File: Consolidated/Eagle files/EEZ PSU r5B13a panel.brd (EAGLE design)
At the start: 337 x 150 mm, 827 parts, among them IC1 LTC3864EMSE#PBF, IC10 DAC8552IDGKTG4, IC11 ADG465SOT-23, IC12 TS5A9411DCKT, IC13 ADS1120IPWR, IC14 LP339D, IC15 TPD4E002DRL, IC16 TPD2E001DZDR, IC17 ADUM3160BRWZ, IC18 TLC5925IDBQR, IC19 Si8641EC-B-IS1, IC2 LP2951SO8, IC20 SI8651EC-B-IS1, IC21 SI8651EC-B-IS1, IC22 LD1117ADT33TR, IC23 Si8641EC-B-IS1, IC24 PCA21125T/Q900/1,1, IC25 AT25256B-SSHL-B, IC26 W5500, IC27 BC857BS, IC28 TLC555, IC29 SN74LVC08APWR, IC3 TL783CKTTR, IC30 SN74LV1T34DBVR, IC31 TPS3705-33D, IC32 SN74LVC2G02DCTR, IC33 74LVC1G125GW.125, IC34 TPA6205A1DGN, IC35 DAC8552IDGKTG4, IC36 ADS1120IPWR, IC37 LTC2050HVCS8#PBF, IC38 TL072D, IC39 TL072D, IC4 LTC3260EMSE#PBF, IC40 REF5025AIDG4, IC41 LTC3864EMSE#PBF, IC42 TS5A9411DCKT, IC43 ADG465SOT-23, IC44 LP339D, IC45 LTC3260EMSE#PBF, IC46 LP2951SO8, IC47 MCP23S17-E/SS, IC48 TL783CKTTR, IC5 TL072D, IC6 TL072D, IC7 LTC2050HVCS8#PBF, IC8 MCP23S17-E/SS, IC9 REF5025AIDG4, J1 BS-244DSM-R, J2 1-726388-2, J3 BS-244DSM-G, J4 BS-244DSM-B, J5 BS-244DSM-R, J6 BS-244DSM-B, J7 693072010801, Q1 IRFR5305, Q10 MMBT5401, Q11 MMBT5551, Q12 MMBT5551, Q13 IRLL2705PBF, Q14 IRFR48ZPBF, Q15 IRLML2246TRPBF, Q16 2N7002, Q17 MMBT5551, Q18 MMBT5401, Q19 MMBT5551, Q2 MMBT5401, Q20 MMBT5551, Q21 BTA26-600, Q22 BTA26-600, Q23 IRLL2705PBF, Q24 2N7002, Q25 2N7002, Q26 IRLML2246TRPBF, Q27 IRLML2246TRPBF, Q28 IRLML2246TRPBF, Q29 IRLML2246TRPBF, Q3 2N7002, Q30 2N7002, Q31 IRLML2246TRPBF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

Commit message: minor change on AUX PS PCB bottom layer
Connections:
- new net +5V2: C80.1, C81.1, D12.C, IC17.16, K_DOUT.A1, OK1.1, OK2.1, OK3.4, TR1.4, X5.10, X5.8
- new net GND7: C80.2, C81.2, C84.2, IC15.2, IC17.15, IC17.9, JP9.3, Q25.2, R118.2, R122.2, R123.1, TR1.3, X10.4, X5.1, X5.2, X5.9
- net +5V: no longer C80.1, C81.1, D12.C, IC17.16, K_DOUT.A1, OK1.1, OK2.1, OK3.4, TR1.4, X5.10, X5.8
- net GND: no longer C80.2, C81.2, C84.2, IC15.2, IC17.15, IC17.9, JP9.3, Q25.2, R118.2, R122.2, R123.1, TR1.3, X10.4, X5.1, X5.2, X5.9
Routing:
- net +5V: track 967.6 -> 836.9 mm, vias 23 -> 20
- net +5V2: track 0.00 -> 130.7 mm, vias 0 -> 3
- net GND7: track 0.00 -> 14.3 mm, vias 0 -> 9
- net GND: track 449.2 -> 434.9 mm, vias 402 -> 393
- net AC_NEUTRAL: track 102.8 -> 101.2 mm
- added copper zone on layer 16, net GND7
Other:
- board text added: "(11/2017)"
- board text added: "EEZ AUX PS r5B13 (11/2017)"
- board text removed: "(09/2017)"
- board text removed: "EEZ AUX PS r5B13 (09/2017)"

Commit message: JP9, JP10 changed to THT
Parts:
- JP10, JP9: value 0R-JUMPA -> ZL303-03P; device jump-0r-smd:A0R-JMP -> EEZ_Lib1:ZL303-03P
- moved JP10 0.60 mm to (45.7, 62.7), turned to 0 degrees
- moved JP9 0.14 mm to (27.0, 64.5), turned to 270 degrees
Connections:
- removed net +5V2: C80.1, C81.1, D12.C, IC17.16, K_DOUT.A1, OK1.1, OK2.1, OK3.4, TR1.4, X5.10, X5.8
- removed net GND7: C80.2, C81.2, C84.2, IC15.2, IC17.15, IC17.9, JP9.3, Q25.2, R118.2, R122.2, R123.1, TR1.3, X10.4, X5.1, X5.2, X5.9
- net +5V: now also C80.1, C81.1, D12.C, IC17.16, K_DOUT.A1, OK1.1, OK2.1, OK3.4, TR1.4, X5.10, X5.8
- net GND: now also C80.2, C81.2, C84.2, IC15.2, IC17.15, IC17.9, JP9.3, Q25.2, R118.2, R122.2, R123.1, TR1.3, X10.4, X5.1, X5.2, X5.9
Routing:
- net +5V: track 836.9 -> 967.6 mm, vias 20 -> 23
- net +5V2: track 130.7 -> 0.00 mm, vias 3 -> 0
- net GND7: track 14.3 -> 0.00 mm, vias 9 -> 0
- net GND: track 434.9 -> 448.1 mm, vias 393 -> 401
- net XUSB_GND: vias 7 -> 6
- removed copper zone on layer 16, net GND7
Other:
- board text added: "EEZ AUX PS r5B13a"
- board text added: "EEZ AUX PS r5B13a (11/2017)"
- board text added: "EEZ Arduino shield (11/2017 r5B13a)"
- board text added: "USB X10"
- board text removed: "EEZ AUX PS r5B13 (11/2017)"
- board text removed: "EEZ Arduino shield (11/2017 r5B13)"
- board text removed: "USB (isolated) X10"

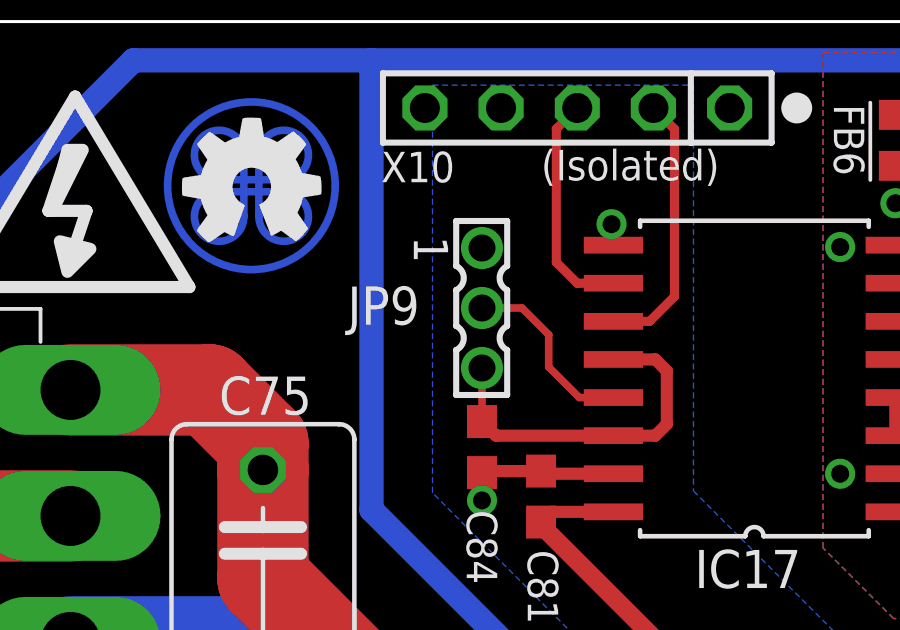
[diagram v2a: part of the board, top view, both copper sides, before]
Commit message: JP9 relocated
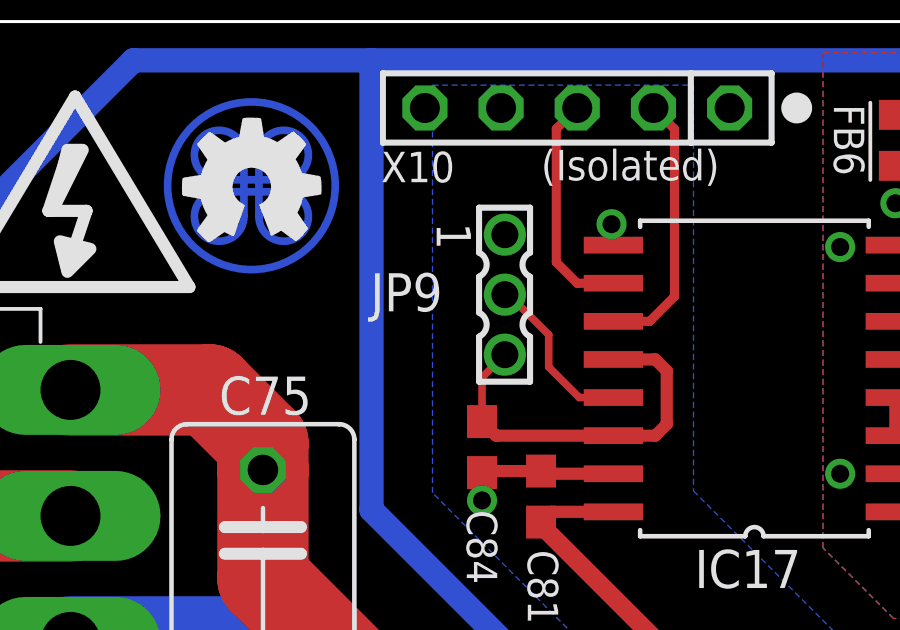
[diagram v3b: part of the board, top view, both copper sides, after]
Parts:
- moved JP9 0.88 mm to (27.7, 64.9)
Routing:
- net N$91: track 12.1 -> 12.8 mm
- net N$105: track 6.25 -> 5.67 mm

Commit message: X1 holes adjustment
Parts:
- D22, D23, D24, D25, D36, D37, D38, D39: device EEZ_Lib1:TO252@1 -> EEZ_Lib1:TO252
- moved X1 4.20 mm to (156.4, 85.8)
- moved X23 4.20 mm to (323.4, 85.8)
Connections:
- new net +5V2: C164.1, C166.2, C186.2, FB10.P$2, IC36.13, IC47.9, Q37.B, Q44.2, R192.2, R193.2, R219.1, R258.2, X21.2
- new net EARTH2: C213.1, C214.2, R270.2, X23.1
- new net GND7: C157.1, C159.1, C161.2, C162.1, C163.1, C164.2, C165.1, C166.1, C167.1, C172.1, C173.2, C177.2, C178.2, C179.1, C180.1, C181.1, C182.1, C183.1, C184.1, C185.1, C186.1, C187.2, C188.2, C189.2, C190.2, C192.2, C193.2, C196.2, C199.2, C200.1, C201.1, C202.2, C204.2, C205.-, C206.-, C207.-, C214.1, C216.1, C217.1, C218.1, C219.1, C220.2, C221.2, C224.1, C225.2, C227.2, C230.2, C231.1, C232.-, C233.+, C234.2, C235.2, C236.-, C237.-, D34.1, D34.2, D38.1, D38.2, D39.1, D39.2, IC35.8, IC36.3, IC36.4, IC36.5, IC36.8, IC40.4, IC41.TP, IC42.3, IC45.14, IC45.17, IC45.2, IC46.4, IC47.10, IC47.15, IC47.16, IC47.17, JP7.3, L9.2, LED1.C, Q43.2, Q45.2, Q51.E, Q52.E, R189.1, R205.1, R213.1, R218.1, R230.2, R234.1, R242.2, R244.1, R246.2, R256.1, R259.1, R267.1, R272.2, R277.1, R278.1, R280.2, R283.2, R286.1, SH4.P$2, SH5.P$2, X21.10, X21.12, X21.14, ZD20.A, ZD21.A
- net +5V: no longer C54.1, C63.2, C64.2, FB1.P$2, IC13.13, IC8.9, Q12.B, Q15.2, R73.1, R84.2, R94.2, R97.2, X2.2
- net +5V1: now also C54.1, C63.2, C64.2, FB1.P$2, IC13.13, IC8.9, Q12.B, Q15.2, R73.1, R84.2, R94.2, R97.2, X2.2; no longer C164.1, C166.2, C186.2, FB10.P$2, IC36.13, IC47.9, Q37.B, Q44.2, R192.2, R193.2, R219.1, R258.2, X21.2
- net EARTH: no longer C2.2, C4.1, R2.2, X1.1
- net EARTH1: now also C2.2, C4.1, R2.2, X1.1; no longer C213.1, C214.2, R270.2, X23.1
- net GND: no longer C10.2, C142.2, C145.-, C146.-, C147.2, C15.2, C16.2, C2.1, C20.2, C21.-, C22.2, C23.-, C24.2, C25.1, C27.-, C28.1, C29.2, C3.2, C30.1, C31.+, C32.2, C33.2, C35.2, C42.1, C43.2, C44.1, C45.1, C46.1, C47.1, C48.1, C49.2, C5.2, C50.1, C51.1, C54.2, C55.2, C56.1, C57.-, C58.2, C59.1, C6.2, C60.1, C61.2, C62.1, C63.1, C64.1, C65.1, C66.1, C67.1, C68.1, C69.1, C72.1, C73.1, C8.2, D1.1, D1.2, D22.1, D22.2, D24.1, D24.2, IC1.TP, IC10.8, IC12.3, IC13.3, IC13.4, IC13.5, IC13.8, IC2.4, IC4.14, IC4.17, IC4.2, IC8.10, IC8.15, IC8.16, IC8.17, IC9.4, JP2.3, L1.2, LED.C, Q16.2, Q17.E, Q19.E, Q7.2, R100.1, R168.2, R18.2, R180.1, R22.2, R23.1, R24.2, R31.2, R45.1, R46.1, R48.1, R66.1, R67.1, R75.1, R86.1, R9.1, R90.1, R91.2, SH1.P$2, SH2.P$2, X2.10, X2.12, X2.14, ZD1.A, ZD16.A
- net GND1: now also C10.2, C142.2, C145.-, C146.-, C147.2, C15.2, C16.2, C2.1, C20.2, C21.-, C22.2, C23.-, C24.2, C25.1, C27.-, C28.1, C29.2, C3.2, C30.1, C31.+, C32.2, C33.2, C35.2, C42.1, C43.2, C44.1, C45.1, C46.1, C47.1, C48.1, C49.2, C5.2, C50.1, C51.1, C54.2, C55.2, C56.1, C57.-, C58.2, C59.1, C6.2, C60.1, C61.2, C62.1, C63.1, C64.1, C65.1, C66.1, C67.1, C68.1, C69.1, C72.1, C73.1, C8.2, D1.1, D1.2, D22.1, D22.2, D24.1, D24.2, IC1.TP, IC10.8, IC12.3, IC13.3, IC13.4, IC13.5, IC13.8, IC2.4, IC4.14, IC4.17, IC4.2, IC8.10, IC8.15, IC8.16, IC8.17, IC9.4, JP2.3, L1.2, LED.C, Q16.2, Q17.E, Q19.E, Q7.2, R100.1, R168.2, R18.2, R180.1, R22.2, R23.1, R24.2, R31.2, R45.1, R46.1, R48.1, R66.1, R67.1, R75.1, R86.1, R9.1, R90.1, R91.2, SH1.P$2, SH2.P$2, X2.10, X2.12, X2.14, ZD1.A, ZD16.A; no longer C157.1, C159.1, C161.2, C162.1, C163.1, C164.2, C165.1, C166.1, C167.1, C172.1, C173.2, C177.2, C178.2, C179.1, C180.1, C181.1, C182.1, C183.1, C184.1, C185.1, C186.1, C187.2, C188.2, C189.2, C190.2, C192.2, C193.2, C196.2, C199.2, C200.1, C201.1, C202.2, C204.2, C205.-, C206.-, C207.-, C214.1, C216.1, C217.1, C218.1, C219.1, C220.2, C221.2, C224.1, C225.2, C227.2, C230.2, C231.1, C232.-, C233.+, C234.2, C235.2, C236.-, C237.-, D34.1, D34.2, D38.1, D38.2, D39.1, D39.2, IC35.8, IC36.3, IC36.4, IC36.5, IC36.8, IC40.4, IC41.TP, IC42.3, IC45.14, IC45.17, IC45.2, IC46.4, IC47.10, IC47.15, IC47.16, IC47.17, JP7.3, L9.2, LED1.C, Q43.2, Q45.2, Q51.E, Q52.E, R189.1, R205.1, R213.1, R218.1, R230.2, R234.1, R242.2, R244.1, R246.2, R256.1, R259.1, R267.1, R272.2, R277.1, R278.1, R280.2, R283.2, R286.1, SH4.P$2, SH5.P$2, X21.10, X21.12, X21.14, ZD20.A, ZD21.A
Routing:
- net +5V: track 967.6 -> 744.0 mm, vias 23 -> 20
- net +5V2: track 0.00 -> 223.6 mm, vias 0 -> 3
- net GND7: track 0.00 -> 185.7 mm, vias 0 -> 139
- net GND: track 448.1 -> 262.5 mm, vias 401 -> 262
- net EARTH2: track 0.00 -> 41.2 mm
- net EARTH: track 325.0 -> 284.0 mm
- added copper zone on layer 1, net GND7
- added copper zone on layer 16, net GND7
- added copper zone on layer 1, net N$273
- added copper zone on layer 1, net N$46
- removed copper zone on layer 1, net N$24
- removed copper zone on layer 1, net N$272 (its old number)

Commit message: #64, #65
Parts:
- removed IC47: MCP23S17-E/SS, EEZ_Lib1:SOP65P780X200-28N
- removed IC48: TL783CKTTR, EEZ_Lib1:TO254P1524X483-4N
- removed LED, LED1: n.c., EEZ_Lib1:LED_HSMH-C170
- removed R283: 1K8, rcl:R0805
- removed R284: 0R082, rcl:R1210
- removed R285: 0R75?, rcl:R1206
- removed R286: 47K, rcl:R0805
- added R78A, R78A1, R78B, R78B1: 470R, rcl:R0805
- added ZD22: SMAJ51A, EEZ_Lib1:DO214AA
- added ZD23: PDZ5.6B, EEZ_Lib1:SOD323-W
- added ZD24: SLVU2.8-TP, EEZ_Lib1:SOT23
- C206, C57: value 10u -> 4u7
- C231, C62: value n.c. -> 10n
- D10, D13, D16, D2, D21, D26, D27, D28, D29, D3, D30, D31, D32, D33, D35, D4, D5, D6, D7, D8, D9: device diode:SOD323-W -> EEZ_Lib1:SOD323-R
- IC11: value ADG465SOT-23 -> DAC8552IDGKTG4; device EEZ_Lib1:SOT95P280X145-6N -> EEZ_Lib1:DGK8-M
- IC35: value DAC8552IDGKTG4 -> ADS1120IPWR; device EEZ_Lib1:DGK8-M -> EEZ_Lib1:PW(R-PDSO-G16)
- IC36: value ADS1120IPWR -> LTC2050HVCS8#PBF; device EEZ_Lib1:PW(R-PDSO-G16) -> EEZ_Lib1:SOIC127P600X173-8N
- IC37: value LTC2050HVCS8#PBF -> TL072D
- IC39: value TL072D -> REF5025AIDG4; device EEZ_Lib1:SOIC127P600X173-8N -> EEZ_Lib1:SOIC127P600X175-8N
- IC40: value REF5025AIDG4 -> LTC3864EMSE#PBF; device EEZ_Lib1:SOIC127P600X175-8N -> EEZ_Lib1:LTC_05-08-1666
- IC41: value LTC3864EMSE#PBF -> TS5A9411DCKT; device EEZ_Lib1:LTC_05-08-1666 -> EEZ_Lib1:SOT65P210X110-6N
- IC42: value TS5A9411DCKT -> LP339D; device EEZ_Lib1:SOT65P210X110-6N -> EEZ_Lib1:SOIC127P600X175-14N
- IC43: value ADG465SOT-23 -> LTC3260EMSE#PBF; device EEZ_Lib1:SOT95P280X145-6N -> EEZ_Lib1:SOP50P490X110-17N
- IC44: value LP339D -> LP2951SO8; device EEZ_Lib1:SOIC127P600X175-14N -> EEZ_Lib1:SOIC127P600X175-8N
- IC45: value LTC3260EMSE#PBF -> MCP23S17-E/SS; device EEZ_Lib1:SOP50P490X110-17N -> EEZ_Lib1:SOP65P780X200-28N
- IC46: value LP2951SO8 -> TL783CKTTR; device EEZ_Lib1:SOIC127P600X175-8N -> EEZ_Lib1:TO254P1524X483-4N
- JP1, JP2, JP3, JP4, JP5, JP6, JP7: value 0R-JUMPA -> JP3-CUT; device jump-0r-smd:A0R-JMP -> EEZ_Lib1:JP3-CUT
- R1, R183, R184, R270: value n.c. -> 10K
- R179: value 0R75? -> 0R75
- R181: value 10K -> n.c.
- R182, R267: value 2K2 -> n.c.
- R185: value 10K -> 10R; device rcl:R0805 -> rcl:R1206
- R187: value 10R -> 2K2; device rcl:R1206 -> rcl:R0805
- R188: value 10K -> 5K6
- R189: value 2K2 -> 5K6
- R190, R191: value 5K6 -> 5K1
- R192, R193: value 5K1 -> 10K
- R196, R197, R214, R257, R258: value 10K -> 220R
- R198: value 220R -> 470R
- R199: value 220R -> 100R
- R200: value 470R -> 1K
- R201: value 100R -> 470R
- R202: value 1K -> 16K
- R203: value 470R -> 750R
- R204: value 16K -> 2K2
- R205: value 750R -> 2K2
- R206: value 2K2 -> 220R
- R207: value 2K2 -> 1K
- R208, R272: value 220R -> 47K
- R209: value 1K -> 10K
- R210, R238, R255: value 47K -> 10K
- R211: value 10K -> 100K
- R213: value 100K -> 220R
- R215: value 220R -> 1K8
- R216: value 220R -> 51K
- R217: value 1K8 -> 100K
- R218: value 51K -> 7K5 0.1%
- R219: value 100K -> 100K 0.1%
- R220: value 7K5 0.1% -> 100K 0.1%
- R221, R222: value 100K 0.1% -> 24K 0.1%
- R223: value 24K 0.1% -> 7K5 0.1%
- R224: value 24K 0.1% -> 3K9 0.1%
- R225: value 7K5 0.1% -> 82R 0.1%
- R226: value 3K9 0.1% -> 82R 0.1%
- R227: value 82R 0.1% -> 3K9 0.1%
- R228: value 82R 0.1% -> 10K
- R229: value 3K9 0.1% -> 0R
- R230: value 10K -> 316K
- R231: value 0R -> 4K7
- R232: value 316K -> 10R; device rcl:R0805 -> rcl:R1206
- R233: value 4K7 -> 100K
- R234: value 10R -> 10K; device rcl:R1206 -> rcl:R0805
- R236, R273, R281: value 10K -> 47K
- R237: value 100K -> R010/2W; device rcl:R0805 -> rcl:R2512
- R239: value R010/2W -> 100R; device rcl:R2512 -> rcl:R0805
- R240: value 10K -> 12K; device rcl:R0805 -> rcl:R1206
- R241: value 100R -> 316K
- R242: value 12K -> 100K; device rcl:R1206 -> rcl:R0805
- R243: value 316K -> 100K
- R244: value 100K -> 10K
- R245: value 1K -> n.c.
- R246: value 100K -> 100R
- R247: value 10K -> 330R
- R248: value n.c. -> 750R
- R249: value 100R -> 1K
- R252: value 1K -> 47K
- R253: value 330R -> 47K
- R254: value 750R -> 10K
- R259, R277: value 47K -> 220R
- R261: value 220R -> 2R2/2W; device rcl:R0805 -> rcl:R2512
- R262: value 220R -> 316K
- R263: value 220R -> 1K
- R264: value 2R2/2W -> 2K2; device rcl:R2512 -> rcl:R0805
- R265: value 316K -> 2K2
- R266: value 1K -> 10R; device rcl:R0805 -> rcl:R1206
- R268: value 2K2 -> n.c.; device rcl:R0805 -> rcl:R1206
- R269: value 10R -> 220R; device rcl:R1206 -> rcl:R0805
- R271: value n.c. -> 1R; device rcl:R1206 -> rcl:R0805
- R274: value 1R -> 16K
- R275: value n.c. -> 5K1
- R276: value 0R030 -> 10K; device EEZ_Lib1:R_2512-4WIRE -> rcl:R0805
- R278: value 47K -> 1K8
- R279: value 16K -> 0R082; device rcl:R0805 -> rcl:R1210
- R280: value 5K1 -> 0R75; device rcl:R0805 -> rcl:R1206
- R282: value 220R -> 0R030; device rcl:R0805 -> rcl:R2512
- R65, R65B, R65B1: device EEZ_Lib1:R_2512-4WIRE -> rcl:R2512
- R78: value 1K -> 2K2
- ZD17: value BZX384-C15 -> PDZ5.6B
- ZD18: value PDZ6.2B -> SLVU2.8-TP; device EEZ_Lib1:SOD323-W -> EEZ_Lib1:SOT23
- ZD19: value n.c. -> BZX384-C15; device EEZ_Lib1:DO214AA -> EEZ_Lib1:SOD323-W
- ZD20: value SMAJ51A -> PDZ6.2B; device EEZ_Lib1:DO214AA -> EEZ_Lib1:SOD323-W
- ZD21: value PDZ5.6B -> n.c.; device EEZ_Lib1:SOD323-W -> EEZ_Lib1:DO214AA
- moved ZD18 208.6 mm to (31.9, 124.8), turned to 180 degrees
- moved IC11 199.3 mm to (230.3, 138.7), turned to 180 degrees
- moved ZD17 191.8 mm to (51.6, 60.1), turned to 270 degrees
- moved R78 183.2 mm to (209.4, 107.9)
- moved R268 126.1 mm to (308.7, 133.6), flipped to the bottom, turned to 180 degrees
- moved R270 117.0 mm to (198.7, 116.3), turned to 180 degrees
- moved R249 106.4 mm to (182.5, 135.7), turned to 180 degrees
- moved R280 101.2 mm to (198.2, 92.7), turned to 270 degrees
- moved ZD19 100.7 mm to (242.2, 81.9), turned to 0 degrees
- moved R278 97.7 mm to (279.1, 138.8), turned to 180 degrees
- moved R281 96.1 mm to (192.8, 93.5), turned to 180 degrees
- moved R279 95.9 mm to (202.2, 90.7), turned to 180 degrees
- moved R248 93.6 mm to (185.7, 98.0), turned to 0 degrees
- moved R277 92.2 mm to (276.9, 135.3), turned to 90 degrees
- moved R266 90.4 mm to (268.6, 78.9), turned to 180 degrees
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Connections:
- removed net +5V2: C164.1, C166.2, C186.2, FB10.P$2, IC36.13, IC47.9, Q37.B, Q44.2, R192.2, R193.2, R219.1, R258.2, X21.2
- removed net EARTH2: C213.1, C214.2, R270.2, X23.1
- removed net GND7: C157.1, C159.1, C161.2, C162.1, C163.1, C164.2, C165.1, C166.1, C167.1, C172.1, C173.2, C177.2, C178.2, C179.1, C180.1, C181.1, C182.1, C183.1, C184.1, C185.1, C186.1, C187.2, C188.2, C189.2, C190.2, C192.2, C193.2, C196.2, C199.2, C200.1, C201.1, C202.2, C204.2, C205.-, C206.-, C207.-, C214.1, C216.1, C217.1, C218.1, C219.1, C220.2, C221.2, C224.1, C225.2, C227.2, C230.2, C231.1, C232.-, C233.+, C234.2, C235.2, C236.-, C237.-, D34.1, D34.2, D38.1, D38.2, D39.1, D39.2, IC35.8, IC36.3, IC36.4, IC36.5, IC36.8, IC40.4, IC41.TP, IC42.3, IC45.14, IC45.17, IC45.2, IC46.4, IC47.10, IC47.15, IC47.16, IC47.17, JP7.3, L9.2, LED1.C, Q43.2, Q45.2, Q51.E, Q52.E, R189.1, R205.1, R213.1, R218.1, R230.2, R234.1, R242.2, R244.1, R246.2, R256.1, R259.1, R267.1, R272.2, R277.1, R278.1, R280.2, R283.2, R286.1, SH4.P$2, SH5.P$2, X21.10, X21.12, X21.14, ZD20.A, ZD21.A
- removed net N$206 (its old number): C176.2, R199.1
- removed net N$269: LED1.A, R275.1
- removed net N$276: IC48.1, R282.2, R283.1
- removed net N$277: R276.2S, R284.1, R65A1.2S, R65B1.2S
- removed net N$278: Q55.2, R227.1, R285.1
- removed net N$78 (its old number): LED.A, R1.1
- removed net N$9 (its old number): IC11.4, IC12.6
- new net N$105: IC38.3, R78.2
- new net N$106: IC37.3, R183.2, R196.2
- new net N$210: D31.C, ZD19.C
- new net N$273: R279.1, R65A1.2S
- new net N$70: R63.1, R65A.2S
- net !DP_DRIVE1: now also R207.1, R212.1; no longer R209.1, R214.1
- net !INT: now also JP3.COM; no longer JP3.2
- net !INT1: now also JP7.COM; no longer JP6.2
- net !PS_DRDY: now also JP3.NC; no longer JP3.3
- net !PS_DRDY1: now also IC35.14, JP7.NC; no longer IC36.14, JP6.3
- net !PS_RESET1: now also IC45.18; no longer IC47.18
- net !SET_100%1: now also IC45.24; no longer IC47.24
- net !SET_DP1: now also IC45.22, R217.2; no longer IC47.22, R219.2
- net +3V3: now also JP4.NO; no longer JP4.3
- net +5V: now also C54.1, C63.2, C64.2, FB1.P$2, IC13.13, IC8.9, JP4.NC, Q12.B, Q15.2, R73.1, R84.2, R94.2, R97.2, X2.2; no longer JP4.1
- net +5V1: now also C164.1, C166.2, C186.2, FB10.P$2, IC35.13, IC45.9, Q37.B, Q44.2, R190.2, R191.2, R217.1, R255.2, X21.2; no longer C54.1, C63.2, C64.2, FB1.P$2, IC13.13, IC8.9, Q12.B, Q15.2, R73.1, R84.2, R94.2, R97.2, X2.2
- net +VNR1: now also IC43.1, IC43.11, IC43.13, IC44.8, IC46.2, IC46.4, R277.1; no longer IC45.1, IC45.11, IC45.13, IC46.8, IC48.2, IC48.4, R282.1
- net +VREF1: now also IC11.2, IC35.9, IC39.6, R270.1; no longer IC35.2, IC36.9, IC40.6, R273.1
- net -12V1: now also IC43.6, R206.2, R207.2; no longer IC45.6, R208.2, R209.2
- net -5VOUT1: now also IC43.5, R262.2; no longer IC45.5, R265.2
- net AC_IN3: now also ZD21.C; no longer ZD19.C
- net AC_IN4: now also R268.2, ZD21.A; no longer R271.2, ZD19.A
- net AUX_ETH_OUT+: now also IC15.3; no longer IC15.1
- net AUX_ETH_OUT-: now also IC15.1; no longer IC15.3
- net AUX_USET_IN: now also R78A.2; no longer R78.2
- net AUX_USET_IN1: now also R78A1.2; no longer R245.2
- net AUX_USET_SW1: now also IC41.1, IC45.25; no longer IC42.1, IC47.25
- net CC_ACTIVE1: now also IC45.23, R189.2, R191.1; no longer IC47.23, R191.2, R193.1
- net CS_ADC1: now also IC35.2; no longer IC36.2
- net CS_DAC1: now also IC11.5; no longer IC35.5
- net CS_EXPANDER1: now also IC45.11; no longer IC47.11
- net CURR_500MA1: now also IC45.2, R273.2; no longer IC47.2, R278.2
- net CURR_50MA1: now also IC45.3, R281.2; no longer IC47.3, R286.2
- net CURR_5A1: now also IC45.1, R272.2; no longer IC47.1, R277.2
- net CV_ACTIVE1: now also IC45.26, R188.2, R190.1; no longer IC47.26, R190.2, R192.1
- net DC_BIAS1: now also R213.2, R214.2, R266.2; no longer R215.2, R216.2, R269.2
- net DC_OUT: no longer R1.2
- net DC_OUT1: now also IC40.11, IC46.3, R237.1, R240.1, R266.1, ZD22.C; no longer IC41.11, IC48.3, R239.1, R242.1, R269.1, R275.2, ZD20.C
- net DP_LED1: now also R212.2; no longer R214.2
- net EARTH: now also C2.2, C4.1, R2.2, X1.1
- net EARTH1: now also C213.1, C214.2, R267.2, X23.1; no longer C2.2, C4.1, R2.2, X1.1
- net FB1: now also IC40.5, R230.2, R231.1, R245.2; no longer IC41.5, R232.2, R233.1, R248.2
- net GCOM: now also JP2.COM; no longer JP2.2
- net GCOM1: now also JP6.COM, R218.1, R224.1; no longer JP7.2, R220.1, R226.1
- net GND: now also C10.2, C142.2, C145.-, C146.-, C147.2, C15.2, C16.2, C2.1, C20.2, C21.-, C22.2, C23.-, C24.2, C25.1, C27.-, C28.1, C29.2, C3.2, C30.1, C31.+, C32.2, C33.2, C35.2, C42.1, C43.2, C44.1, C45.1, C46.1, C47.1, C48.1, C49.2, C5.2, C50.1, C51.1, C54.2, C55.2, C56.1, C57.-, C58.2, C59.1, C6.2, C60.1, C61.2, C62.1, C63.1, C64.1, C65.1, C66.1, C67.1, C68.1, C69.1, C72.1, C73.1, C8.2, D1.1, D1.2, D22.1, D22.2, D24.1, D24.2, IC1.TP, IC10.8, IC12.3, IC13.3, IC13.4, IC13.5, IC13.8, IC2.4, IC4.14, IC4.17, IC4.2, IC8.10, IC8.15, IC8.16, IC8.17, IC9.4, JP2.NO, L1.2, Q16.2, Q17.E, Q19.E, Q7.2, R100.1, R168.2, R18.2, R180.1, R22.2, R23.1, R24.2, R31.2, R45.1, R46.1, R48.1, R66.1, R67.1, R75.1, R86.1, R9.1, R90.1, R91.2, SH1.P$2, SH2.P$2, X2.10, X2.12, X2.14, ZD1.A, ZD16.A, ZD18.1, ZD18.2
- net GND1: now also C157.1, C159.1, C161.2, C162.1, C163.1, C164.2, C165.1, C166.1, C167.1, C172.1, C173.2, C177.2, C178.2, C179.1, C180.1, C181.1, C182.1, C183.1, C184.1, C185.1, C186.1, C187.2, C188.2, C189.2, C190.2, C192.2, C193.2, C196.2, C199.2, C200.1, C201.1, C202.2, C204.2, C205.-, C206.-, C207.-, C214.1, C216.1, C217.1, C218.1, C219.1, C220.2, C221.2, C224.1, C225.2, C227.2, C230.2, C231.1, C232.-, C233.+, C234.2, C235.2, C236.-, C237.-, D34.1, D34.2, D38.1, D38.2, D39.1, D39.2, IC11.8, IC35.3, IC35.4, IC35.5, IC35.8, IC39.4, IC40.TP, IC41.3, IC43.14, IC43.17, IC43.2, IC44.4, IC45.10, IC45.15, IC45.16, IC45.17, JP6.NO, L9.2, Q43.2, Q45.2, Q51.E, Q52.E, R187.1, R203.1, R211.1, R216.1, R228.2, R232.1, R240.2, R242.1, R243.2, R253.1, R256.1, R264.1, R269.2, R272.1, R273.1, R275.2, R278.2, R281.1, SH4.P$2, SH5.P$2, X21.10, X21.12, X21.14, ZD22.A, ZD23.A, ZD24.1, ZD24.2; no longer C10.2, C142.2, C145.-, C146.-, C147.2, C15.2, C16.2, C2.1, C20.2, C21.-, C22.2, C23.-, C24.2, C25.1, C27.-, C28.1, C29.2, C3.2, C30.1, C31.+, C32.2, C33.2, C35.2, C42.1, C43.2, C44.1, C45.1, C46.1, C47.1, C48.1, C49.2, C5.2, C50.1, C51.1, C54.2, C55.2, C56.1, C57.-, C58.2, C59.1, C6.2, C60.1, C61.2, C62.1, C63.1, C64.1, C65.1, C66.1, C67.1, C68.1, C69.1, C72.1, C73.1, C8.2, D1.1, D1.2, D22.1, D22.2, D24.1, D24.2, IC1.TP, IC10.8, IC12.3, IC13.3, IC13.4, IC13.5, IC13.8, IC2.4, IC4.14, IC4.17, IC4.2, IC8.10, IC8.15, IC8.16, IC8.17, IC9.4, JP2.3, L1.2, LED.C, Q16.2, Q17.E, Q19.E, Q7.2, R100.1, R168.2, R18.2, R180.1, R22.2, R23.1, R24.2, R31.2, R45.1, R46.1, R48.1, R66.1, R67.1, R75.1, R86.1, R9.1, R90.1, R91.2, SH1.P$2, SH2.P$2, X2.10, X2.12, X2.14, ZD1.A, ZD16.A
- net HEATSINK1: now also R267.1; no longer R270.1
- net INT_EXP: now also JP3.NO; no longer JP3.1
- net INT_EXP1: now also IC45.20, JP7.NO; no longer IC47.20, JP6.1
- net ISENSE+1: now also IC36.3, R224.2, R225.2; no longer IC37.3, R226.2, R227.2
- net ISENSE-1: now also IC36.2, R226.2, R227.1; no longer IC37.2, R228.2, R229.1
- net I_MON1: now also IC36.6, R1.1, R227.2, R258.1; no longer IC37.6, R181.1, R229.2, R261.1
- net I_SERVO1: now also IC38.1, R210.1; no longer IC39.1, R212.1
- net I_SET1: now also IC11.3, R260.1, R78.1; no longer IC35.3, R182.1, R263.1
- net LOOP_CTRL1: now also R198.1; no longer R200.1
- net L_OUT12: now also R230.1, R234.1, R235.1, R246.1; no longer R232.1, R236.1, R237.1, R249.1
- net MODE: now also JP1.COM; no longer JP1.2
- net MODE1: now also IC40.1, JP5.COM; no longer IC41.1, JP5.2
- net N$102: now also JP4.COM; no longer JP4.2
- net N$104: now also R78A.1, R78B.2; no longer R63.1, R65.2S, R65A.2S, R65B.2S
- net N$12: now also IC12.6, R78B.1, ZD18.3; no longer IC11.1, R78.1
- net N$157: now also C160.1, D27.C, IC37.2, R184.2, R197.2; no longer IC39.3, R182.2
- net N$159: now also C165.2, C185.2, IC35.12; no longer IC38.3, R198.2
- net N$16: now also JP2.NC; no longer JP2.1
- net N$168: now also IC42.1, IC42.2, R188.1; no longer C160.1, D27.C, IC38.2, R186.2, R199.2
- net N$179: now also IC37.5, R192.2, R218.2, R219.1; no longer C165.2, C185.2, IC36.12, R187.2
- net N$180: now also IC37.6, R193.2, R220.1, R223.2; no longer IC44.1, IC44.2, R190.1
- net N$189: now also C171.1, R222.1; no longer IC38.5, R194.2, R221.1
- net N$190: now also C169.1, R219.2, R221.1; no longer IC38.6, R195.2, R222.1, R225.2
- net N$191: now also C168.2, R192.1; no longer C171.1, R222.2, R224.1
- net N$192: now also C170.2, R193.1; no longer C169.1, R221.2, R223.1
- net N$196: now also C174.2, R195.1; no longer C168.2, R194.1
- net N$200: no longer R65.1S, R65B.1S
- net N$202: now also D26.C, IC38.2, R1.2, R194.2, R195.2; no longer C170.2, R195.1
- net N$203: now also C175.2, R196.1; no longer C174.2, R197.1
- net N$204: now also C176.2, R197.1; no longer D26.C, IC39.2, R181.2, R196.2, R197.2
- net N$205: now also D30.C, D32.A, Q35.G, R200.1; no longer C175.2, R198.1
- net N$209: now also D31.A, Q36.1, R199.1, R201.2; no longer D30.C, D32.A, Q35.G, R202.1
- net N$211: now also C177.1; no longer D31.A, Q36.1, R203.2
- net N$212: now also D32.C, ZD20.C; no longer D31.C, ZD17.C
- net N$213: now also Q45.3, R204.1, R205.1, R261.1; no longer C177.1, R203.1
- net N$214: now also D33.A, Q42.C, Q45.1, R205.2; no longer D32.C, ZD18.C
- net N$215: now also Q41.E, R198.2; no longer Q45.3, R206.1, R207.1, R264.1
- net N$216: now also IC42.13, IC42.14, R189.1; no longer D33.A, Q42.C, Q45.1, R207.2
- net N$217: now also IC42.5, IC42.6, R209.2; no longer Q41.E, R200.2
- net N$218: now also IC42.11, IC42.8, R210.2; no longer IC44.13, IC44.14, R191.1
- net N$219: now also IC42.7, IC42.9, R187.2, R208.1; no longer IC44.5, IC44.6, R211.2
- net N$220: now also IC42.10, IC42.4, R186.2, R228.1; no longer IC44.11, IC44.8, R212.2
- net N$221: now also Q40.E, R213.1; no longer IC44.7, IC44.9, R189.2, R210.1
- net N$222: now also Q39.E, R214.1; no longer IC44.10, IC44.4, R188.2, R230.1
- net N$223: now also Q37.E, R215.2; no longer Q40.E, R215.1
- net N$224: now also Q41.B, R202.1, R203.2, R264.2; no longer Q39.E, R216.1
- net N$225: now also Q38.3, R206.1; no longer Q37.E, R217.2
- net N$226: now also Q42.B, R204.2; no longer Q41.B, R204.1, R205.2, R267.2
- net N$227: now also C187.1, IC39.5; no longer Q38.3, R208.1
- net N$228: now also IC38.6, IC38.7, JP6.NC; no longer Q42.B, R206.2
- net N$229: now also C160.2, R229.1; no longer C187.1, IC40.5
- net N$230: now also C191.2, R232.2; no longer IC39.6, IC39.7, JP7.1
- net N$231: now also C209.2, D35.A, Q46.B, R233.1, R235.2; no longer C160.2, R231.1
- net N$232: now also D35.C, Q46.E; no longer C191.2
- net N$233: now also C195.1, IC40.6, R238.2; no longer C209.2, D35.A, Q46.B, R235.1, R237.2
- net N$234: now also C194.1, R238.1; no longer D35.C, Q46.E, R236.2
- net N$235: now also C197.1, IC40.9; no longer C195.1, IC41.6, R240.2
- net N$236: now also IC40.12, R271.1; no longer C194.1, R240.1
- net N$237: now also IC40.2, R236.1; no longer C197.1, IC41.9
- net N$238: now also C198.2, IC40.4; no longer IC41.12, R274.1
- net N$239: now also C209.1, Q46.C, Q48.3, R245.1; no longer IC41.2, R238.1
- net N$240: now also C222.1, L6.1, L7.2, R239.1, R246.2; no longer C198.2, IC41.4
- net N$241: now also C204.1, C232.+, FB9.P$1, IC43.12, R241.1; no longer C209.1, Q46.C, Q48.3, R248.1
- net N$242: now also C231.2, IC41.6, R78B1.1, ZD24.3; no longer C222.1, L6.1, L7.2, R241.1, R249.2
- net N$243: now also IC40.8, R244.1; no longer C204.1, C232.+, FB9.P$1, IC45.12, R243.1
- net N$244: now also C210.2, Q50.B, R247.1, R248.2, R265.2; no longer IC42.6, IC43.4
- net N$245: now also C212.2, Q50.C, R252.1, R254.2; no longer C231.2, IC43.1, R245.1
- net N$246: now also Q49.C, R249.1; no longer IC41.8, R247.1
- net N$247: now also C211.1, Q49.B, R250.2, R251.1; no longer C210.2, Q50.B, R250.1, R251.2, R268.2
- net N$248: now also C212.1, Q51.B, R252.2, R253.2; no longer C212.2, Q50.C, R255.1, R257.2
- net N$249: now also Q52.B, R254.1, R256.2; no longer Q49.C, R252.1
- net N$250: now also C217.2, IC35.10, R257.2; no longer C211.1, Q49.B, R253.2, R254.1
- net N$251: now also C218.2, IC35.7, R258.2; no longer C212.1, Q51.B, R255.2, R256.2
- net N$252: now also C219.2, IC35.11; no longer Q52.B, R257.1
- net N$253: now also C220.1, IC35.6; no longer C217.2, IC36.10
- net N$254: now also R194.1, R263.2; no longer C218.2, IC36.7, R261.2
- net N$255: now also C158.1, R263.1; no longer C219.2, IC36.11, R262.2
- net N$256: now also R249.2, R265.1; no longer C220.1, IC36.6, R263.2
- net N$257: now also C229.2, R268.1; no longer R196.1, R266.2
- net N$258: now also C230.1, IC38.5, R269.1, R270.2; no longer C158.1, R266.1
- net N$259: now also Q47.1, R271.2; no longer R252.2, R268.1
- net N$260: now also IC43.15, R241.2, R243.1; no longer C229.2, R271.1
- net N$261: now also C200.2, IC43.16; no longer C230.1, IC39.5, R272.1, R273.2
- net N$262: now also C201.2, IC43.3; no longer Q47.1, R274.2
- net N$263: now also IC43.4, R242.2, R262.1; no longer IC45.15, R243.2, R246.1
- net N$264: now also C203.1, IC43.10, IC43.9; no longer C200.2, IC45.16
- net N$265: now also C203.2, IC43.7, IC43.8; no longer C201.2, IC45.3
- net N$266: now also Q54.3, R282.2, R65A1.2, R65B1.2; no longer IC45.4, R244.2, R265.1
- net N$267: now also IC44.7, R274.2, R275.1; no longer C203.1, IC45.10, IC45.9
- net N$268: now also C236.+, FB10.P$1, IC44.1, R274.1, R276.1; no longer C203.2, IC45.7, IC45.8
- net N$270: now also R226.1, R65A1.1S; no longer Q54.3, R276.2, R65A1.2, R65B1.2
- net N$271: now also Q53.3, R280.2; no longer IC46.7, R280.1
- net N$272: now also R277.2, R278.1; no longer C236.+, FB10.P$1, R279.1, R281.1
- net N$274: now also Q55.2, R225.1, R280.1; no longer R228.1, R276.1S, R65A1.1S, R65B1.1S
- net N$275: now also R78A1.1, R78B1.2; no longer Q53.3, R284.2, R285.2
- net OUT+1: now also R181.1, R200.2, R233.2, R247.2, R261.2, ZD19.A; no longer R183.1, R204.2, R235.2, R250.2, R264.2, ZD17.A
- net OUT-1: now also R182.2, R250.1; no longer R184.2, R253.1
- net POST_OE1: now also R215.1; no longer R217.1
- net POUT-1: now also R282.1; no longer R276.1
- net PREG_OUT1: now also R239.2; no longer R241.2
- net PRE_OE1: now also IC45.28, R211.2, R244.2; no longer IC47.28, R213.2, R247.2
- net PS_MISO1: now also IC35.15, IC45.14; no longer IC36.15, IC47.14
- net PS_MOSI1: now also IC11.7, IC35.16, IC45.13; no longer IC35.7, IC36.16, IC47.13
- net PS_SCLK1: now also IC11.6, IC35.1, IC45.12; no longer IC35.6, IC36.1, IC47.12
- net PWRGOOD1: now also IC44.5, IC45.27, R276.2; no longer IC46.5, IC47.27, R281.2
- net Q9C1: now also ZD20.A; no longer ZD18.A
- net SENSE+1: now also R181.2, R221.2, R248.1; no longer R183.2, R223.2, R251.1
- net SENSE-1: now also R182.1, R222.2, R251.2; no longer R184.1, R224.2, R254.2
- net SENSE1: now also IC40.10, R237.2; no longer IC41.10, R239.2
- net SENSE_ERR1: now also IC45.21, R255.1; no longer IC47.21, R258.1
- net SENSE_PROT1: now also R199.2, R216.2; no longer R201.2, R218.2
- net SGND: now also JP1.NO; no longer JP1.1
- net SGND1: now also IC40.3, JP5.NO, R231.2, R236.2; no longer IC41.3, JP5.1, R233.2, R238.2
- net SYNC: now also JP1.NC; no longer JP1.3
- net SYNC3: now also JP5.NC; no longer JP5.3
- net U_MON1: now also IC37.7, R184.1, R223.1, R257.1; no longer IC38.7, R186.1, R225.1, R260.1
- net U_SERVO1: now also IC37.1, R209.1, R229.2; no longer IC38.1, R211.1, R231.2
- net U_SET1: now also IC11.4, IC41.4; no longer IC35.4, IC42.4
- net U_SET_OUT1: now also IC41.5, R183.1, R259.1; no longer IC42.5, R185.1, R262.1
- net V+: no longer IC11.6
- net V+1: now also IC11.1, IC36.7, IC37.8, IC39.2, IC41.2, IC42.3, R185.1, R208.2, ZD23.C; no longer IC35.1, IC37.7, IC39.8, IC40.2, IC42.2, IC43.6, IC44.3, R187.1, R210.2, ZD21.C
- net V-: no longer IC11.3
- net V-1: now also IC36.4, IC42.12, R186.1; no longer IC39.4, IC43.3, IC44.12, R188.1
- net XUSB_GND: now also ZD17.A
- net XUSB_VBUS: now also ZD17.C
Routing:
- net +5V: track 744.0 -> 970.5 mm, vias 20 -> 23
- net +5V2: track 223.6 -> 0.00 mm, vias 3 -> 0
- net GND7: track 185.7 -> 0.00 mm, vias 139 -> 0
- net GND: track 262.5 -> 402.9 mm, vias 262 -> 390
- net N$218: track 3.90 -> 55.5 mm, vias 0 -> 4
- net GND1: track 185.7 -> 138.3 mm, vias 139 -> 129
- net N$220: track 55.5 -> 11.0 mm, vias 4 -> 0
- net EARTH: track 284.0 -> 327.8 mm
- net N$245: track 4.92 -> 46.7 mm, vias 0 -> 2
- net EARTH2: track 41.2 -> 0.00 mm
- net N$248: track 46.7 -> 6.27 mm, vias 2 -> 0
- net N$242: track 4.74 -> 43.9 mm, vias 0 -> 2
- net N$9 (its old number): track 39.0 -> 0.00 mm, vias 2 -> 0
- net N$12: track 4.92 -> 43.9 mm, vias 0 -> 2
- net N$247: track 44.0 -> 7.10 mm, vias 2 -> 0
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- added copper zone on layer 1, net N$236
- added copper zone on layer 1, net N$240
- added copper zone on layer 1, net N$241
- added copper zone on layer 1, net N$264
- added copper zone on layer 1, net N$265
- added copper zone on layer 1, net N$266
- added copper zone on layer 1, net N$269
- added copper zone on layer 1, net N$9
- removed copper zone on layer 1, net GND7
- removed copper zone on layer 16, net GND7
- removed copper zone on layer 1, net N$238
- removed copper zone on layer 1, net N$242
- removed copper zone on layer 1, net N$243
- removed copper zone on layer 1, net N$267
- removed copper zone on layer 1, net N$268
- removed copper zone on layer 1, net N$270
- removed copper zone on layer 1, net N$273
- removed copper zone on layer 1, net N$46 (its old number)
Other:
- board text added: "(07/2018 r5B13a)"
- board text added: "EEZ Arduino shield (07/2018 r5B13a)"
- board text added: "EEZ PSU power board (07/2018 r5B13a)"
- board text added: "R78A"
- board text added: "R78B"
- board text added: "TR1"
- board text added: "ZD17"
- board text added: "ZD18"
- board text added: "r5B13a (07/2018)"
- board text removed: "(09/2017 r5B13)"
- board text removed: "EEZ Arduino shield (11/2017 r5B13a)"
- board text removed: "EEZ PSU power board (09/2017 r5B13)"
- board text removed: "IC11"
- board text removed: "LED"
- board text removed: "R1"
- board text removed: "R78"
- board text removed: "r5B13 (11/2017)"
